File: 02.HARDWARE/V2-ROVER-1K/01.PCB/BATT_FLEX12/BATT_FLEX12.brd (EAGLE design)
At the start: 24 x 18.1 mm, 8 parts, among them K1 FLEX6, K2 FLEX6, K3 FLEX8, K4 FLEX8, K5 FLEX6, K6 FLEX6, K7 FLEX8, K8 FLEX8

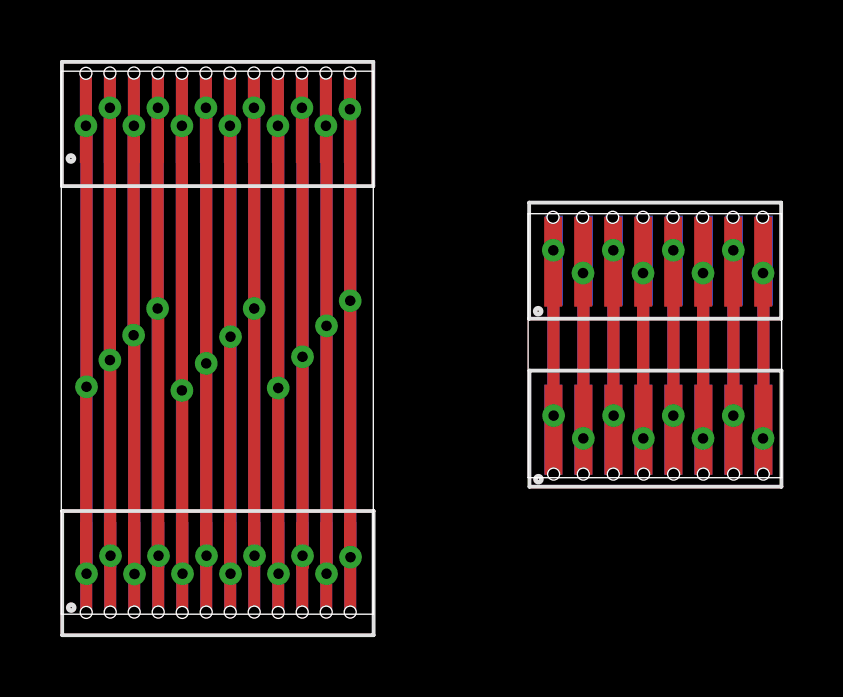
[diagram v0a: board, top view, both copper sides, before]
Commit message: Release PROTO-SETI
Se separan los flex en dos PCBs distintos: flex8 y flex12
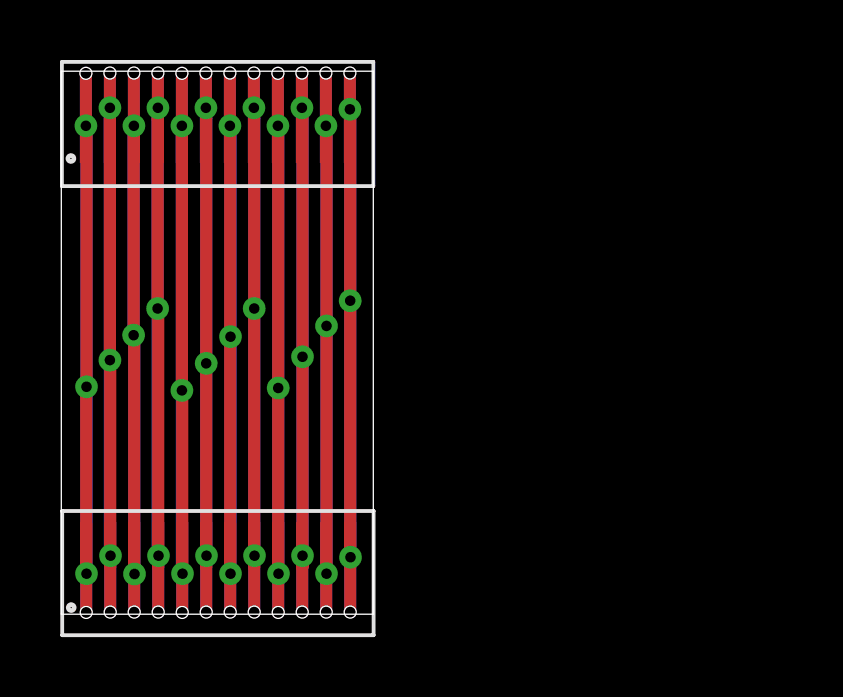
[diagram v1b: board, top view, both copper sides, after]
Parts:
- removed K3, K4, K7, K8: FLEX8, Flex_3mm:FLEX8
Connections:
- removed net F8-1: K3.1, K4.1, K7.1, K8.1
- removed net F8-2: K3.2, K4.2, K7.2, K8.2
- removed net F8-3: K3.3, K4.3, K7.3, K8.3
- removed net F8-4: K3.4, K4.4, K7.4, K8.4
- removed net F8-5: K3.5, K4.5, K7.5, K8.5
- removed net F8-6: K3.7, K4.7, K7.7, K8.7
- removed net F8-7: K3.8, K4.8, K7.8, K8.8
- removed net F8-8: K3.9, K4.9, K7.9, K8.9
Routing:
- net F8-6: track 11.9 -> 0.00 mm, vias 2 -> 0
- net F8-5: track 11.7 -> 0.00 mm, vias 2 -> 0
- net F8-1: track 11.7 -> 0.00 mm, vias 2 -> 0
- net F8-3: track 11.6 -> 0.00 mm, vias 2 -> 0
- net F8-2: track 11.5 -> 0.00 mm, vias 2 -> 0
- net F8-8: track 11.3 -> 0.00 mm, vias 2 -> 0
- net F8-7: track 11.3 -> 0.00 mm, vias 2 -> 0
- net F8-4: track 11.3 -> 0.00 mm, vias 2 -> 0
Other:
- board size 24 x 18.1 mm -> 10.4 x 18.1 mm
